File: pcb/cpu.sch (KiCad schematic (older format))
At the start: 34 parts, among them P27 BDM, U1 MC9S12XDP512, Y1 16MHz

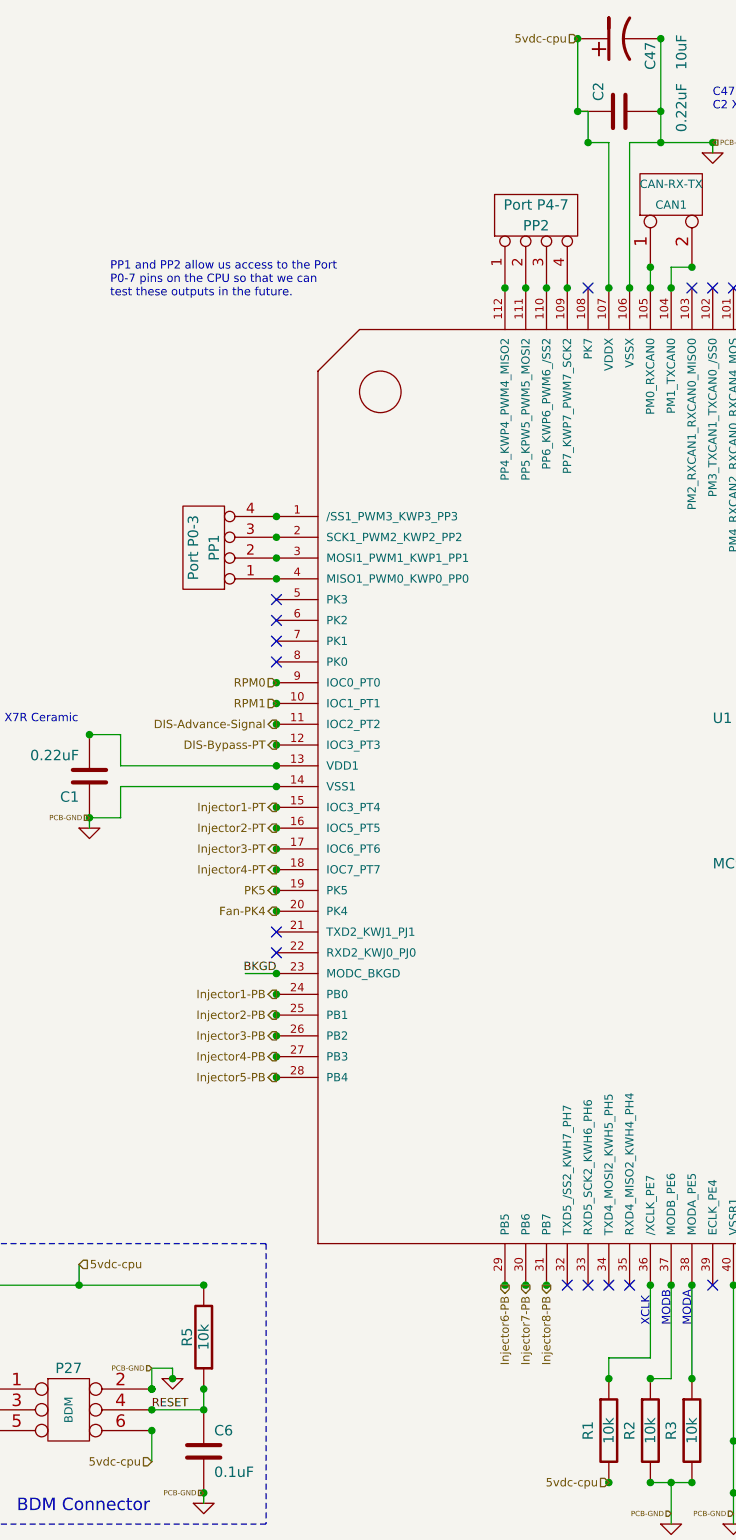
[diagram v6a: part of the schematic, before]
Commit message: Started laying out PCB changes for SO-8 high side driver and new SO-8 low side drivers.
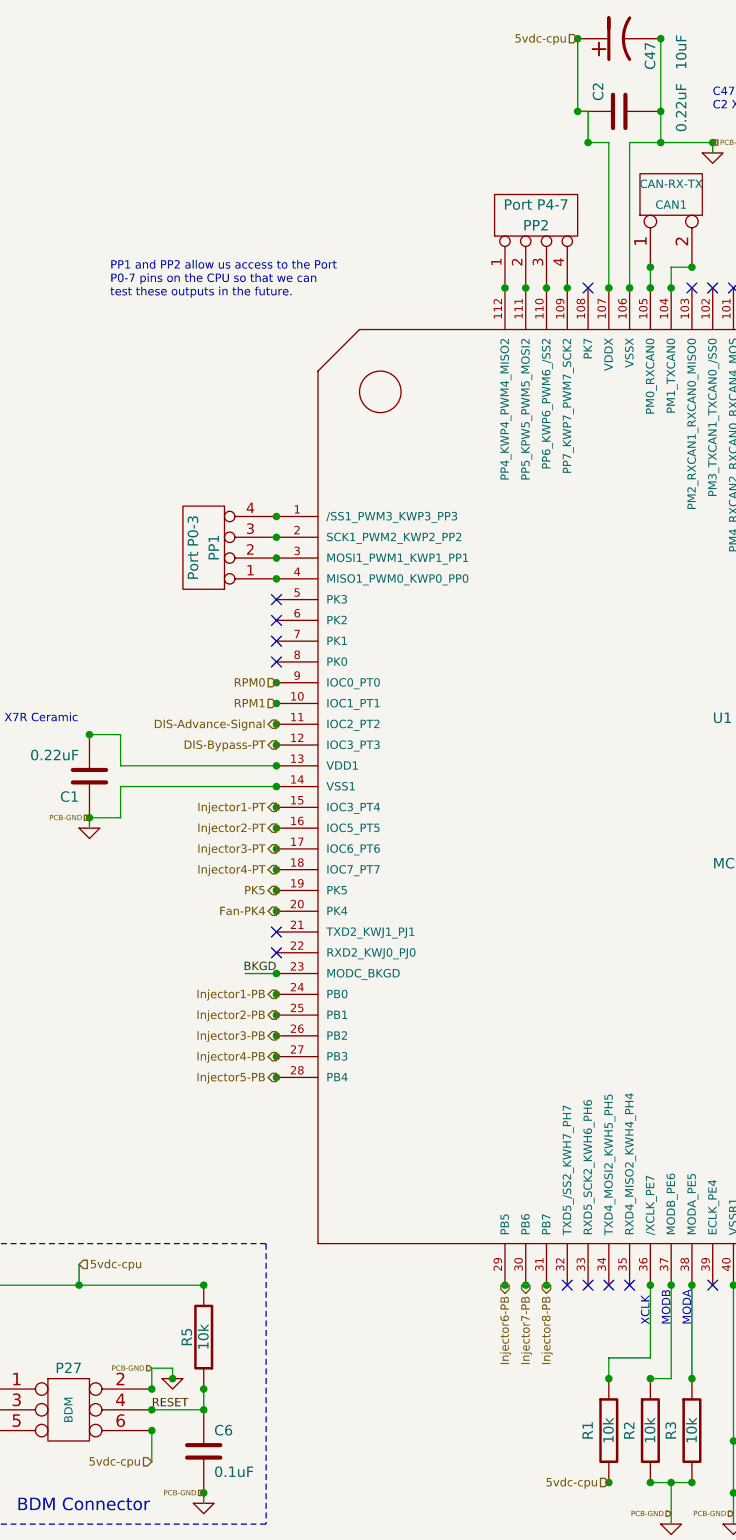
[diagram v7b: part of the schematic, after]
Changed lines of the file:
@@
 Sheet 2 7
 Title "Jaguar PCB for FreeEMS"
-Date "5 feb 2014"
+Date "4 mar 2014"
 Rev "0.7-alpha"
 Comp "Git: xxxxxxxxxx"
@@
 Connection ~ 7000 4550
 Connection ~ 5200 6550
-Connection ~ 1600 7050
 Wire Wire Line
 	8400 6350 7900 6350
@@
 	3700 900  3650 900
 Wire Wire Line
-	3700 900  3700 1050
+	3700 1050 3700 900
 Connection ~ 3700 1050
 Wire Wire Line
@@
 $EndComp
 $Comp
-L GND #PWR02
+L GND #PWR2
 U 1 1 4F1D6CA4
 P 1300 4350
-F 0 "#PWR02" H 1300 4350 30  0001 C CNN
+F 0 "#PWR2" H 1300 4350 30  0001 C CNN
 F 1 "GND" H 1300 4280 30  0001 C CNN
 F 2 "" H 1300 4350 60  0001 C CNN
@@
 $EndComp
 $Comp
-L GND #PWR03
+L GND #PWR8
 U 1 1 4F1C316A
 P 5200 6850
-F 0 "#PWR03" H 5200 6850 30  0001 C CNN
+F 0 "#PWR8" H 5200 6850 30  0001 C CNN
 F 1 "GND" H 5200 6780 30  0001 C CNN
 F 2 "" H 5200 6850 60  0001 C CNN
@@
 $EndComp
 $Comp
-L GND #PWR04
+L GND #PWR11
 U 1 1 4F1C3153
 P 8450 6000
-F 0 "#PWR04" H 8450 6000 30  0001 C CNN
+F 0 "#PWR11" H 8450 6000 30  0001 C CNN
 F 1 "GND" H 8450 5930 30  0001 C CNN
 F 2 "" H 8450 6000 60  0001 C CNN
@@
 $EndComp
 $Comp
-L GND #PWR05
+L GND #PWR3
 U 1 1 4F1C290C
 P 1700 7000
-F 0 "#PWR05" H 1700 7000 30  0001 C CNN
+F 0 "#PWR3" H 1700 7000 30  0001 C CNN
 F 1 "GND" H 1700 6930 30  0001 C CNN
 F 2 "" H 1700 7000 60  0001 C CNN
@@
 $EndComp
 $Comp
-L GND #PWR06
+L GND #PWR4
 U 1 1 4F1C2905
 P 1850 7600
-F 0 "#PWR06" H 1850 7600 30  0001 C CNN
+F 0 "#PWR4" H 1850 7600 30  0001 C CNN
 F 1 "GND" H 1850 7530 30  0001 C CNN
 F 2 "" H 1850 7600 60  0001 C CNN
@@
 $EndComp
 $Comp
-L GND #PWR07
+L GND #PWR6
 U 1 1 4F1C289E
 P 4300 1100
-F 0 "#PWR07" H 4300 1100 30  0001 C CNN
+F 0 "#PWR6" H 4300 1100 30  0001 C CNN
 F 1 "GND" H 4300 1030 30  0001 C CNN
 F 2 "" H 4300 1100 60  0001 C CNN
@@
 $EndComp
 $Comp
-L GND #PWR08
+L GND #PWR12
 U 1 1 4F1C287C
 P 8950 1000
-F 0 "#PWR08" H 8950 1000 30  0001 C CNN
+F 0 "#PWR12" H 8950 1000 30  0001 C CNN
 F 1 "GND" H 8950 930 30  0001 C CNN
 F 2 "" H 8950 1000 60  0001 C CNN
@@
 $EndComp
 $Comp
-L GND #PWR09
+L GND #PWR9
 U 1 1 4F1C2863
 P 6100 1850
-F 0 "#PWR09" H 6100 1850 30  0001 C CNN
+F 0 "#PWR9" H 6100 1850 30  0001 C CNN
 F 1 "GND" H 6100 1780 30  0001 C CNN
 F 2 "" H 6100 1850 60  0001 C CNN
@@
 $EndComp
 $Comp
-L GND #PWR010
+L GND #PWR13
 U 1 1 4F1C284A
 P 8950 5300
-F 0 "#PWR010" H 8950 5300 30  0001 C CNN
+F 0 "#PWR13" H 8950 5300 30  0001 C CNN
 F 1 "GND" H 8950 5230 30  0001 C CNN
 F 2 "" H 8950 5300 60  0001 C CNN
@@
 $EndComp
 $Comp
-L GND #PWR011
+L GND #PWR10
 U 1 1 4F1C2831
 P 8100 4450
-F 0 "#PWR011" H 8100 4450 30  0001 C CNN
+F 0 "#PWR10" H 8100 4450 30  0001 C CNN
 F 1 "GND" H 8100 4380 30  0001 C CNN
 F 2 "" H 8100 4450 60  0001 C CNN
@@
 $EndComp
 $Comp
-L GND #PWR012
+L GND #PWR14
 U 1 1 4F1C2808
 P 9950 6850
-F 0 "#PWR012" H 9950 6850 30  0001 C CNN
+F 0 "#PWR14" H 9950 6850 30  0001 C CNN
 F 1 "GND" H 9950 6780 30  0001 C CNN
 F 2 "" H 9950 6850 60  0001 C CNN
@@
 XCLK
 $Comp
-L GND #PWR013
+L GND #PWR7
 U 1 1 4F1C2798
 P 4400 7700
-F 0 "#PWR013" H 4400 7700 30  0001 C CNN
+F 0 "#PWR7" H 4400 7700 30  0001 C CNN
 F 1 "GND" H 4400 7630 30  0001 C CNN
 F 2 "" H 4400 7700 60  0001 C CNN
@@
 $EndComp
 $Comp
-L GND #PWR014
+L GND #PWR5
 U 1 1 4F1C273A
 P 4100 7700
-F 0 "#PWR014" H 4100 7700 30  0001 C CNN
+F 0 "#PWR5" H 4100 7700 30  0001 C CNN
 F 1 "GND" H 4100 7630 30  0001 C CNN
 F 2 "" H 4100 7700 60  0001 C CNN
